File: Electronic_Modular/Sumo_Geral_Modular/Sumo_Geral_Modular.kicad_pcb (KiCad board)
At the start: 2 copper layers, 42 parts, among them J1 Conn_01x02, J10 Conn_01x03, J11 Conn_01x03, J12 USB_B_Micro, J13 SENSOR DE MOUSE, J14 ALIMENTAÇÃO SDM, J15 MPU, J2 VL53L0X 1, J3 VL53L0X 2, J4 VL53L0X 3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

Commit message: shore: update PCB
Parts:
- added R9: 10K, Resistor_SMD:R_0201_0603Metric, F.Cu at (113.3, 55.1)
- J1: value Conn_01x02 -> Bateria
- J10: value Conn_01x03 -> ESC1
- J11: value Conn_01x03 -> ESC2
- J8, J9: footprint Connector_PinSocket_2.54mm:PinSocket_1x02_P2.54mm_Vertical -> Connector_JST:JST_XH_B2B-XH-AM_1x02_P2.50mm_Vertical
- moved R1 80.9 mm to (137.8, 28.3), turned to -90 degrees
- moved R2 80.0 mm to (137.8, 31.5), turned to 90 degrees
- moved J2 76.8 mm to (145.9, 27.8), turned to -90 degrees
- moved SW1 74.4 mm to (94.7, 24.0)
- moved J3 73.1 mm to (145.9, 43.8), turned to -90 degrees
- moved J4 70.2 mm to (145.9, 59.7), turned to -90 degrees
- moved D3 69.9 mm to (127.7, 48.4), turned to 90 degrees
- moved SW3 68.0 mm to (127.8, 61.2), turned to 90 degrees
- moved C5 67.2 mm to (111.0, 27.6), turned to 90 degrees
- moved SW2 62.3 mm to (106.8, 31.3), turned to -90 degrees
- moved R8 61.6 mm to (127.7, 46.2), turned to -90 degrees
- moved J13 58.5 mm to (137.5, 91.2), turned to 180 degrees
- moved D1 56.5 mm to (94.5, 33.1), turned to 90 degrees
- moved J1 54.6 mm to (83.8, 39.4), turned to 90 degrees
- moved C6 54.0 mm to (116.2, 55.2), turned to 90 degrees
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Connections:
- C5 pad 1: EN -> GND
- C5 pad 2: GND -> EN
- C6 pad 1: 3V3 -> I00
- J8 pad 1: AO1 -> AO2
- J8 pad 2: AO2 -> AO1
- SW3 pad 1: 3V3 -> I00

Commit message: shore: PCB review
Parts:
- added R10: 10K, Resistor_SMD:R_0201_0603Metric, F.Cu at (106.6, 39.8)
- added R11: 10K, Resistor_SMD:R_0201_0603Metric, F.Cu at (106.6, 41.5)
- added R12: 10K, Resistor_SMD:R_0201_0603Metric, F.Cu at (106.6, 43.3)
- U4: footprint RF_Module:ESP32-WROOM-32UE -> RF_Module:ESP32-WROOM-32
- moved J15 3.20 mm to (147.0, 74.6)
- moved C1 2.34 mm to (101.4, 34.8)
- moved D1 2.34 mm to (94.2, 35.4)
- moved R3 2.34 mm to (94.2, 33.8)
- moved U2 2.34 mm to (98.1, 50.3)
- moved C5 2.34 mm to (110.7, 29.9)
- moved SW1 2.34 mm to (94.4, 26.3)
- moved SW2 2.34 mm to (106.5, 33.6)
- moved C2 2.34 mm to (98.4, 44.5)
- moved C3 2.34 mm to (98.5, 46.0)
- moved U1 2.34 mm to (98.1, 40.0)
- moved D2 1.89 mm to (95.4, 54.6)
- moved C4 1.70 mm to (99.1, 55.7)
- moved C7 0.72 mm to (95.5, 57.5)
- moved U4 0.30 mm to (122.1, 33.6)
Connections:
- U4 pad 16: unconnected-(U4-IO13-Pad16) -> INT
- U4 pad 5: unconnected-(U4-SENSOR_VN-Pad5) -> DDT
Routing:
- net SCL: track 0.00 -> 68.0 mm
- net SDA: track 0.00 -> 63.4 mm
- net SS/CS: track 0.00 -> 52.7 mm
- net XSH3: track 0.00 -> 49.1 mm, vias 0 -> 1
- net RXD0: track 0.00 -> 44.8 mm
- net XSH2: track 0.00 -> 41.2 mm, vias 0 -> 1
- net XSH1: track 0.00 -> 35.1 mm, vias 0 -> 1
- net I00: track 0.00 -> 26.4 mm
- net Net-(J12-D+): track 0.00 -> 16.1 mm
- net Net-(Q1-E): track 0.00 -> 13.7 mm
- net EN: track 0.00 -> 12.3 mm
- net Net-(J12-D-): track 0.00 -> 9.78 mm
- net AO2: track 0.00 -> 9.73 mm
- net AO1: track 0.00 -> 9.71 mm
- net Net-(Q2-E): track 0.00 -> 9.46 mm
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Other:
- board outline added: 67.5 x 70.1 mm

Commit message: shore: schematic final review
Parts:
- added C8: C_Polarized, Capacitor_SMD:C_0603_1608Metric, F.Cu at (84.6, 75.5)
- added D4: 1N4007, Diode_SMD:D_0603_1608Metric, F.Cu at (58.5, 59.0)
- added D5: LED, LED_SMD:LED_0603_1608Metric, F.Cu at (58.5, 61.6)
- added R13: 1K, Resistor_SMD:R_0603_1608Metric, F.Cu at (62.5, 61.5)
- added R14: 10K, Resistor_SMD:R_0603_1608Metric, F.Cu at (89.3, 75.4)
- C1, C2, C3, C4, C7: footprint Capacitor_SMD:C_0201_0603Metric -> Capacitor_SMD:C_0603_1608Metric
- C5, C6: value 10uF -> 100nF; footprint Capacitor_SMD:C_0201_0603Metric -> Capacitor_SMD:C_0603_1608Metric
- D1, D3: footprint LED_SMD:LED_0201_0603Metric -> LED_SMD:LED_0603_1608Metric
- D2: value D -> 1N4007; footprint Diode_SMD:D_0201_0603Metric -> Diode_SMD:D_0603_1608Metric
- J13: value SENSOR DE MOUSE -> ADSN-9500
- J14: value ALIMENTAÇÃO SDM -> PS ADSN-9500
- J15: value MPU -> MPU-6050
- J5: footprint Connector_PinHeader_2.54mm:PinHeader_1x03_P2.54mm_Vertical -> Connector_PinHeader_2.00mm:PinHeader_1x03_P2.00mm_Vertical
- J8: value Conn_01x02 -> MA
- J9: value Conn_01x02 -> MB
- Q1, Q2: footprint Package_TO_SOT_THT:TO-92_Inline -> Package_TO_SOT_SMD:SOT-23
- R1, R11, R12, R2, R3, R4, R5, R6, R7, R8, R9: footprint Resistor_SMD:R_0201_0603Metric -> Resistor_SMD:R_0603_1608Metric
- R10: footprint Resistor_SMD:R_0201_0603Metric -> Capacitor_SMD:C_0603_1608Metric
- SW1: value SW_Push -> ON/OFF
- SW2: value SW_Push -> EN; footprint Button_Switch_SMD:SW_SPST_TL3342 -> Button_Switch_SMD:SW_SPST_TL3305C
- SW3: value SW_Push -> BOOT; footprint Button_Switch_SMD:SW_SPST_TL3342 -> Button_Switch_SMD:SW_SPST_TL3305C
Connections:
- net BO1 renamed Net-(J6-Pin_7)
- net BO2 renamed Net-(J6-Pin_6)
- C2 pad 1: 5V -> Net-(D4-A)
- J6 pad 4: AO1 -> Net-(J6-Pin_4)
- J6 pad 5: AO2 -> Net-(J6-Pin_5)
- J8 pad 1: AO2 -> Net-(J6-Pin_4)
- J8 pad 2: AO1 -> Net-(J6-Pin_5)
- R4 pad 1: TXD0 -> RXD0
- R5 pad 1: RXD0 -> TXD0
- R6 pad 2: Net-(Q1-E) -> Net-(Q2-E)
- R7 pad 2: Net-(Q2-E) -> Net-(Q1-E)
- U1 pad 2: 5V -> Net-(D4-A)
- U3 pad 13: Net-(Q1-E) -> Net-(Q2-E)
- U3 pad 14: Net-(Q2-E) -> Net-(Q1-E)
- U4 pad 11: MOTION -> BIN1
- U4 pad 12: XSH3 -> BIN2
- U4 pad 13: BIN1 -> AIN1
- U4 pad 14: BIN2 -> ESC 1
- U4 pad 16: INT -> ESC 2
- U4 pad 23: SS/CS -> MOTION
- U4 pad 26: unconnected-(U4-IO4-Pad26) -> XSH1
- U4 pad 27: ESC 2 -> XSH2
- U4 pad 28: ESC 1 -> XSH3
- U4 pad 29: unconnected-(U4-IO5-Pad29) -> SS/CS
- U4 pad 6: XSH1 -> INT
- U4 pad 7: XSH2 -> IR
- U4 pad 8: IR -> unconnected-(U4-IO32-Pad8)
- U4 pad 9: AIN1 -> unconnected-(U4-IO33-Pad9)
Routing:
- net (no net): track 0.00 -> 19.4 mm
- net AO2: track 9.73 -> 0.00 mm
- net AO1: track 9.71 -> 0.00 mm

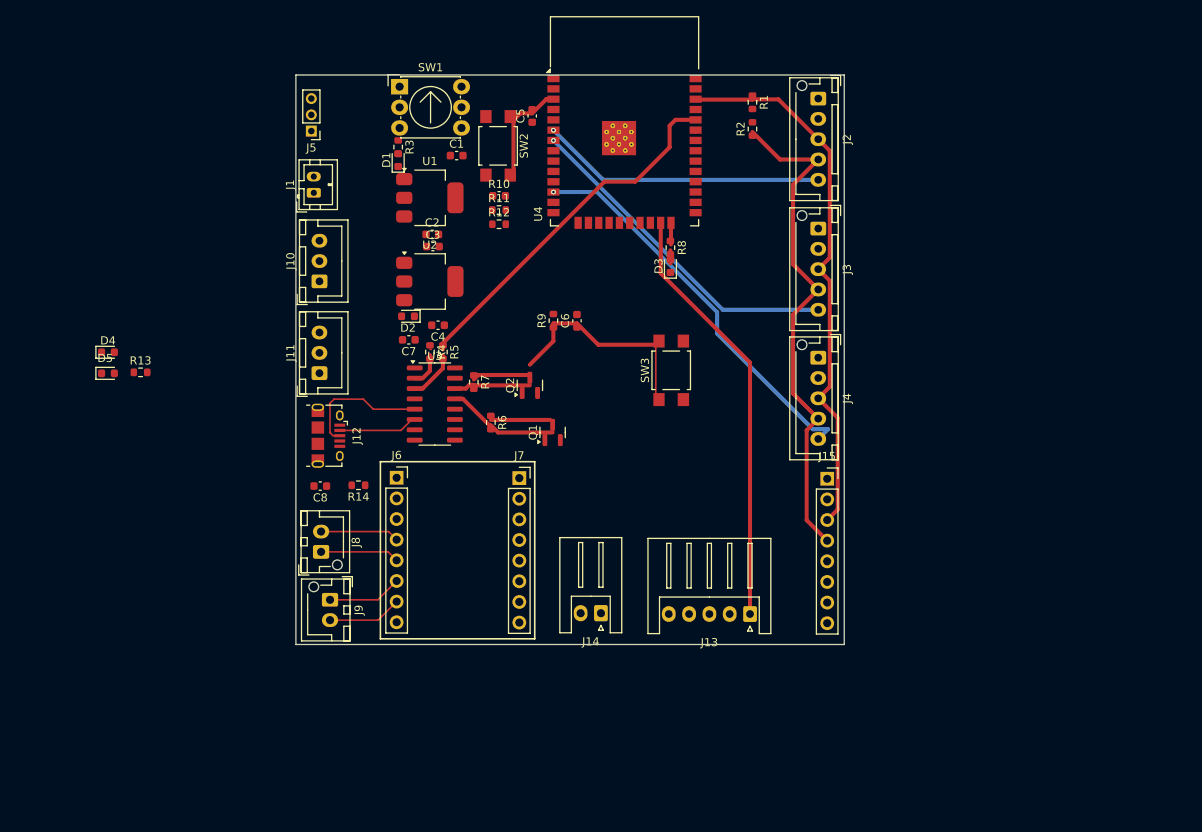
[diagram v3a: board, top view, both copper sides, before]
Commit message: chore: Add/Update 3D models on PCB
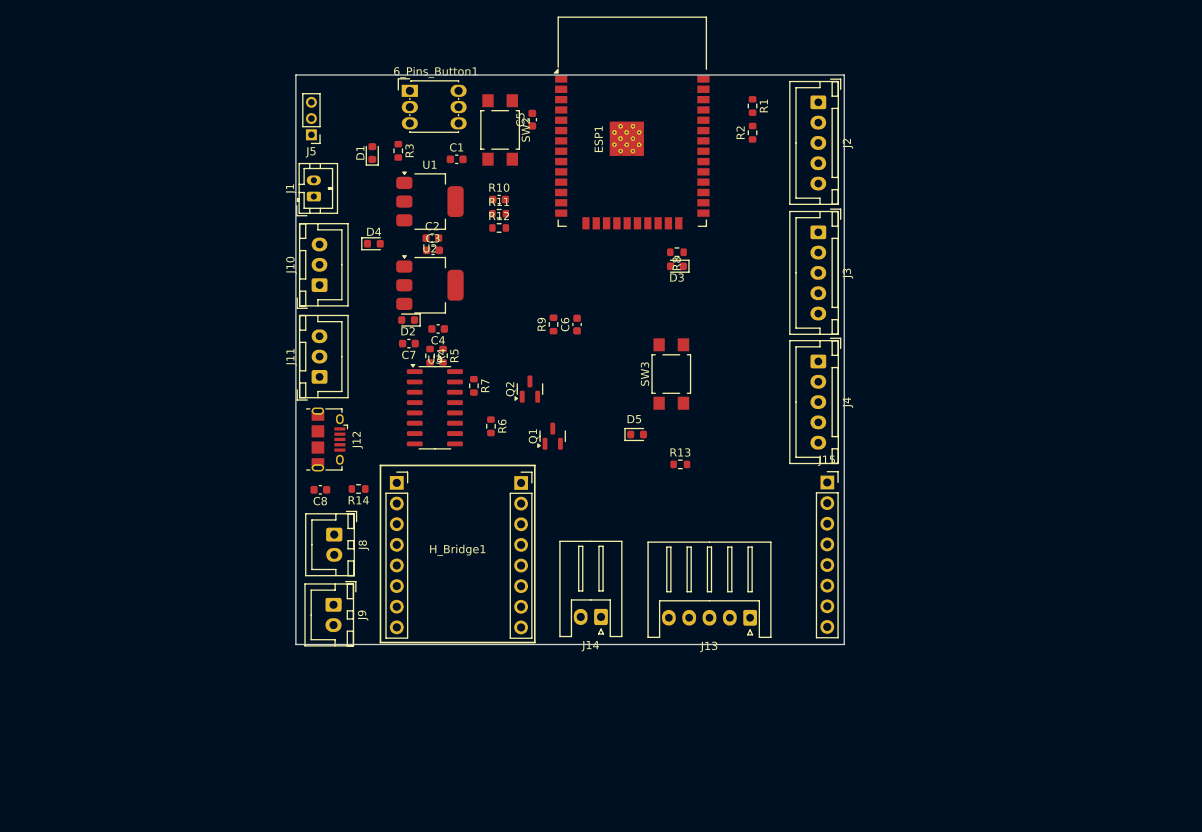
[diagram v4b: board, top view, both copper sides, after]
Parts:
- removed J6: ponte H ld e, Connector_PinSocket_2.54mm:PinSocket_1x08_P2.54mm_Vertical
- removed J7: ponte H ld d, Connector_PinSocket_2.54mm:PinSocket_1x08_P2.54mm_Vertical
- removed SW1: ON/OFF, Button_Switch_THT:Nidec_Copal_SH-7010C
- removed U4: ESP32-WROOM-32UE, RF_Module:ESP32-WROOM-32
- added 6_Pins_Button1: ON/OFF, esp32_devkit_v1_doit:Push_Button_6_pins, F.Cu at (95.6, 26.8)
- added ESP1: ESP32-WROOM­32UE, RF_Module:ESP32-WROOM-32, F.Cu at (123.0, 33.6)
- added H_Bridge1: ~, esp32_devkit_v1_doit:H_Bridge_with_headers, F.Cu at (101.5, 83.8)
- D1: value LED -> BLUE
- D3, D5: value LED -> RED
- J2, J3, J4: footprint Connector_JST:JST_XH_B5B-XH-AM_1x05_P2.50mm_Vertical -> Connector_JST:JST_XH_B5B-XH-A_1x05_P2.50mm_Vertical
- J8: value MA -> Motor A; footprint Connector_JST:JST_XH_B2B-XH-AM_1x02_P2.50mm_Vertical -> Connector_JST:JST_XH_B2B-XH-A_1x02_P2.50mm_Vertical
- J9: value MB -> Motor B; footprint Connector_JST:JST_XH_B2B-XH-AM_1x02_P2.50mm_Vertical -> Connector_JST:JST_XH_B2B-XH-A_1x02_P2.50mm_Vertical
- R13: value 1K -> 130R
- R3: value 1K -> 500R
- moved R13 67.4 mm to (128.9, 72.8)
- moved D5 65.6 mm to (123.6, 69.2)
- moved D4 35.4 mm to (91.2, 45.7)
- moved D1 3.30 mm to (91.0, 34.5)
- moved J8 2.68 mm to (86.3, 81.5), turned to -90 degrees
- moved SW2 1.97 mm to (106.7, 31.7)
- moved R8 0.98 mm to (128.5, 46.7), turned to 180 degrees
- moved D3 0.80 mm to (128.5, 48.4), turned to 180 degrees
- moved J9 0.75 mm to (86.2, 90.1)
- moved J12 0.46 mm to (85.6, 69.8)
- moved J15 0.46 mm to (147.0, 75.1)
- moved C3 0.46 mm to (98.5, 46.5)
- moved C5 0.46 mm to (110.7, 30.4)
- moved C7 0.46 mm to (95.5, 58.0)
- moved J1 0.46 mm to (83.8, 39.9)
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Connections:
- Q2 pad 3: I00 -> IO0
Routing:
- net SCL: track 68.0 -> 0.00 mm
- net SDA: track 63.4 -> 0.00 mm
- net SS/CS: track 52.7 -> 0.00 mm
- net XSH3: track 49.1 -> 0.00 mm, vias 1 -> 0
- net RXD0: track 44.8 -> 0.00 mm
- net XSH2: track 41.2 -> 0.00 mm, vias 1 -> 0
- net XSH1: track 35.1 -> 0.00 mm, vias 1 -> 0
- net I00: track 26.4 -> 0.00 mm
- net (no net): track 19.4 -> 0.00 mm
- net Net-(J12-D+): track 16.1 -> 0.00 mm
- net Net-(Q1-E): track 13.7 -> 0.00 mm
- net EN: track 12.3 -> 0.00 mm
- net Net-(J12-D-): track 9.78 -> 0.00 mm
- net Net-(Q2-E): track 9.46 -> 0.00 mm
- net Net-(H_Bridge1-BO1): track 9.16 -> 0.00 mm
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
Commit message: chore: change PCB size
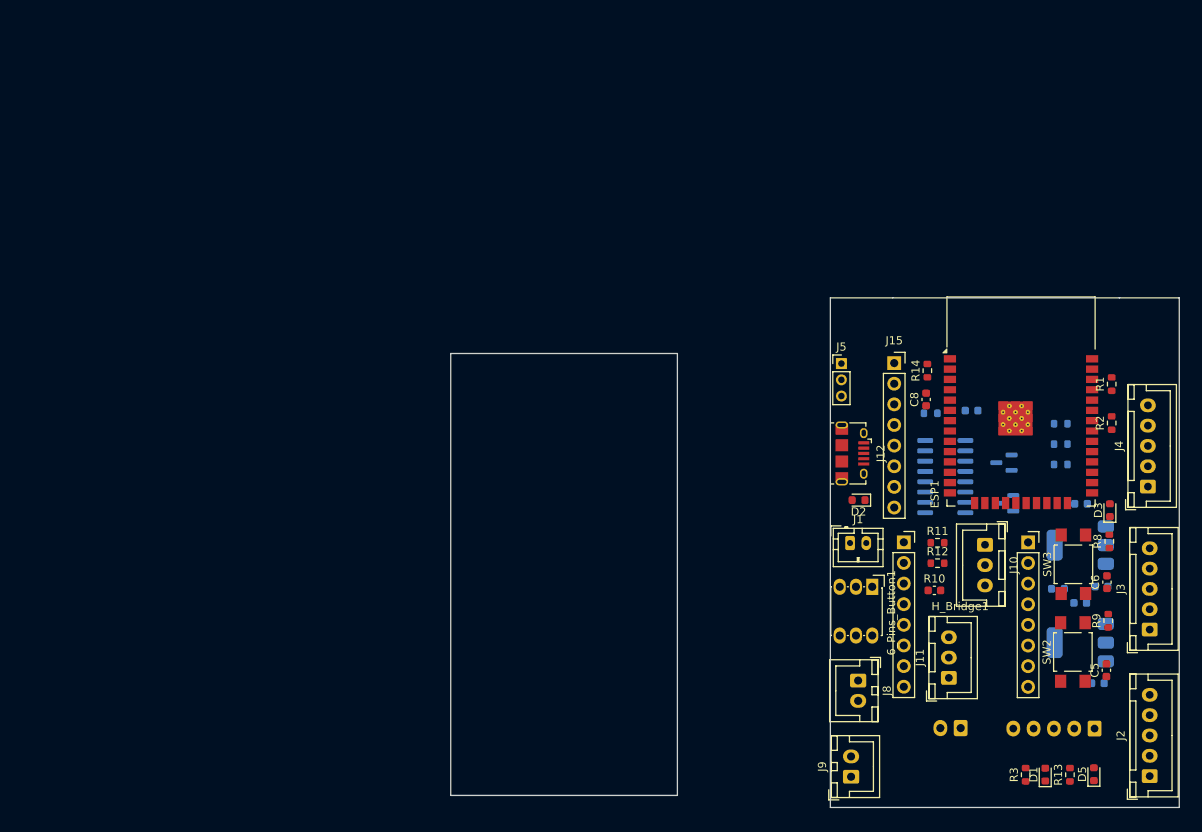
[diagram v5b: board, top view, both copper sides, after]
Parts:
- C1, C2, C3, C4, C7, D4, J13, Q1, Q2, R4, R5, R6, R7, U1, U2, U3: moved to B.Cu
- C8: value C_Polarized -> 100nF
- J14: value PS ADSN-9500 -> ADSN-9500-PS; moved to B.Cu
- moved D1 112.8 mm to (173.8, 111.0)
- moved R3 108.9 mm to (171.4, 111.0), turned to 90 degrees
- moved C2 98.6 mm to (180.3, 99.8), turned to 180 degrees
- moved C5 97.9 mm to (181.4, 98.2)
- moved U1 96.7 mm to (178.2, 94.8), turned to 180 degrees
- moved SW2 95.4 mm to (177.2, 95.9), turned to 90 degrees
- moved D4 94.3 mm to (175.4, 88.1), turned to 180 degrees
- moved C1 94.2 mm to (178.2, 89.9), turned to 180 degrees
- moved J2 92.4 mm to (186.7, 111.2), turned to 90 degrees
- moved J10 87.9 mm to (166.4, 82.7), turned to -90 degrees
- moved C4 87.6 mm to (180.8, 87.9)
- moved U2 86.2 mm to (178.2, 82.8), turned to 180 degrees
- moved J11 85.9 mm to (162.0, 99.1)
- moved C3 85.7 mm to (178.2, 77.7), turned to 180 degrees
- moved 6_Pins_Button1 83.5 mm to (152.5, 87.9), turned to -90 degrees
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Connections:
- net 2s renamed BAT
- ESP1 pad 38: unconnected-(ESP1-GND-Pad38) -> GND
- H_Bridge1 pad 3: unconnected-(H_Bridge1-GND-Pad3) -> GND
- H_Bridge1 pad 9: unconnected-(H_Bridge1-GND-Pad9) -> GND
- R1 pad 1: SCL -> 3V3
- R1 pad 2: 3V3 -> SCL
- R14 pad 1: 3V3 -> EN
- R14 pad 2: EN -> 3V3
- R2 pad 1: SDA -> 3V3
- R2 pad 2: 3V3 -> SDA
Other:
- board size 67.5 x 70.1 mm -> 89.7 x 62.7 mm

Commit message: chore: finish PCB V1
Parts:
- D2, J12: moved to B.Cu
- moved J1 27.8 mm to (150.9, 110.3), turned to -90 degrees
- moved 6_Pins_Button1 18.2 mm to (148.6, 105.7), turned to 90 degrees
- moved R10 16.9 mm to (157.8, 71.6), turned to -90 degrees
- moved J9 16.6 mm to (150.1, 94.7)
- moved R7 15.9 mm to (165.1, 61.0), turned to 0 degrees
- moved J8 15.9 mm to (151.2, 83.5)
- moved R11 14.2 mm to (157.8, 68.5), turned to -90 degrees
- moved Q2 14.1 mm to (165.6, 63.9), turned to 0 degrees
- moved R4 12.6 mm to (170.3, 73.4), turned to -90 degrees
- moved Q1 11.7 mm to (170.0, 61.0)
- moved C3 11.4 mm to (182.0, 88.4), turned to 0 degrees
- moved C2 10.9 mm to (175.3, 90.1)
- moved R12 10.5 mm to (157.8, 74.8), turned to -90 degrees
- moved C1 10.3 mm to (180.5, 99.9)
- moved C7 9.08 mm to (166.8, 75.1), turned to 90 degrees
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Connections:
- C6 pad 1: I00 -> IO0
- ESP1 pad 10: AIN2 -> AIN1
- ESP1 pad 12: BIN2 -> ESC 1
- ESP1 pad 13: AIN1 -> ESC 2
- ESP1 pad 14: ESC 1 -> BIN2
- ESP1 pad 16: ESC 2 -> AIN2
- ESP1 pad 5: DDT -> IR
- ESP1 pad 6: INT -> DDT
- ESP1 pad 7: IR -> INT
- R9 pad 1: I00 -> IO0
- SW3 pad 1: I00 -> IO0
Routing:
- net 3V3: track 0.00 -> 209.4 mm, vias 0 -> 3
- net SDA: track 0.00 -> 108.5 mm
- net SCL: track 0.00 -> 101.7 mm
- net BAT: track 0.00 -> 85.0 mm, vias 0 -> 2
- net 5V: track 0.00 -> 79.0 mm
- net EN: track 0.00 -> 60.5 mm, vias 0 -> 1
- net MOSI: track 0.00 -> 51.8 mm, vias 0 -> 1
- net MISO: track 0.00 -> 47.9 mm, vias 0 -> 1
- net SS/CS: track 0.00 -> 47.4 mm, vias 0 -> 1
- net SCLK: track 0.00 -> 45.8 mm, vias 0 -> 1
- net IO0: track 0.00 -> 44.9 mm, vias 0 -> 1
- net MOTION: track 0.00 -> 38.0 mm, vias 0 -> 1
- net XSH1: track 0.00 -> 29.6 mm
- net BIN1: track 0.00 -> 24.3 mm
- net ESC 2: track 0.00 -> 24.2 mm
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- added copper zone on B.Cu, net GND
- added copper zone on F.Cu, net GND
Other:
- board size 89.7 x 62.7 mm -> 43 x 62.7 mm
- board text added: "*"
- board text added: "+"
- board text added: "3V3"
- board text added: "5V"
- board text added: "BATTERY"
- board text added: "BOOT"
- board text added: "CL"
- board text added: "CS"
- board text added: "ESC-1"
- board text added: "ESC-2"
- board text added: "GND"
- board text added: "GND S"
- board text added: "MI"
- board text added: "MO"
- board text added: "MODULAR BOARD MINI SUMO V1"
- board text added: "MT"
- board text added: "ON/OFF"
- board text added: "PROJECT NEON 11/2024"
- board text added: "RESET"
- board text added: "SCL"
- board text added: "SDA"
- board text added: "XSHUT"

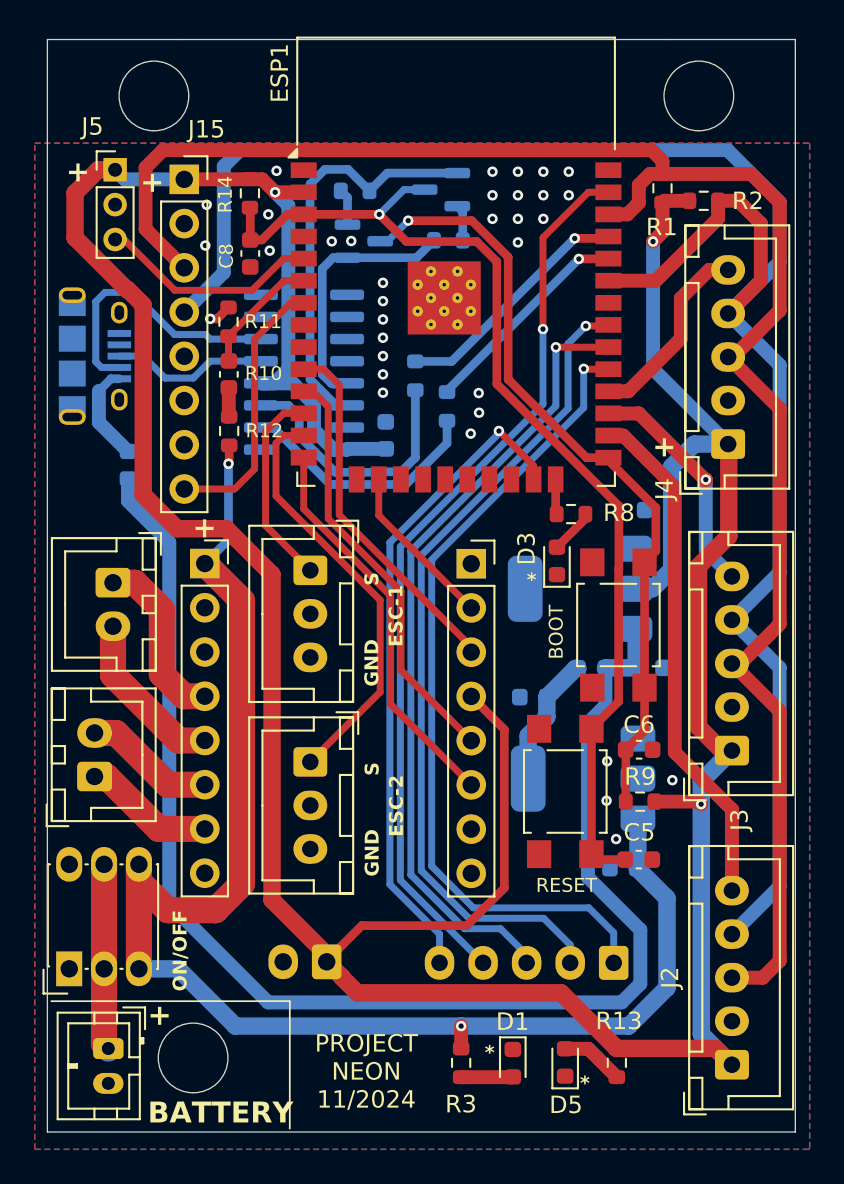
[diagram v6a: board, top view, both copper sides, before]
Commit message: chore: application of DRC and error correction
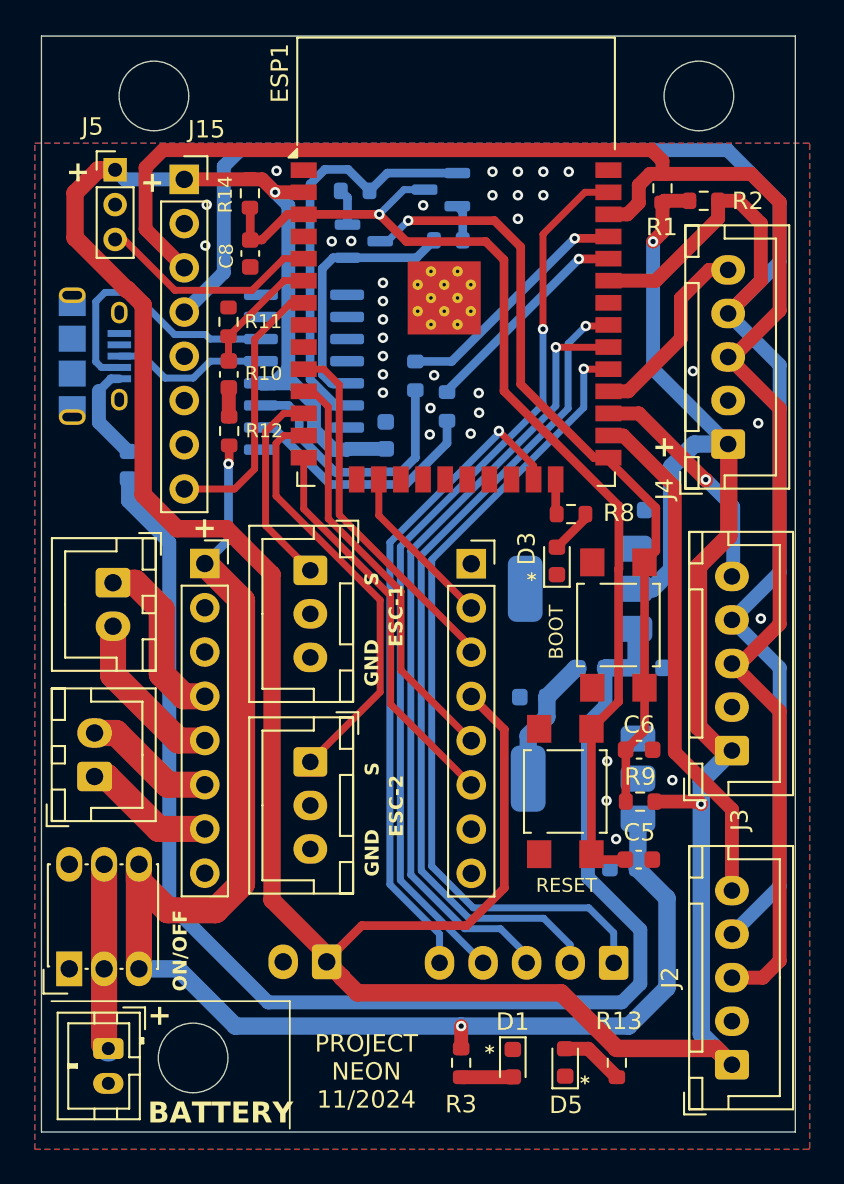
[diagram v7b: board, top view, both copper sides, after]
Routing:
- net GND: track 1.32 -> 0.00 mm
- net IO0: track 44.9 -> 45.5 mm
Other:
- board size 43 x 62.7 mm -> 43.3 x 62.9 mm
